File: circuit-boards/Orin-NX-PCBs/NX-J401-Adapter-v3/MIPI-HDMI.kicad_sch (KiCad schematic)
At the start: 2 parts, among them J10 MIPI, J11 HDMI

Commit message: Interim checkin of NX Adapter board
Signed-off-by: Scott Berman <scott.berman@bluerivertech.com>
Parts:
- J11: footprint NX-J401-Adapter:HDMI_A_Molex_208658-1001_Horizontal -> NX-J401-Adapter:SWITCHCRAFT_RAVHD19ETR; DIST P/N 900-2086581051CT-ND -> 137-RAVHD19ECT-ND; MFG Molex -> Switchcraft; MFG P/N 2086581051 -> RAVHD19ETR
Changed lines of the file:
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@@
 			)
 		)
-		(property "Footprint" "NX-J401-Adapter:HDMI_A_Molex_208658-1001_Horizontal"
+		(property "Footprint" "NX-J401-Adapter:SWITCHCRAFT_RAVHD19ETR"
 			(at 278.765 120.65 0)
 			(effects
@@
 			)
 		)
-		(property "Datasheet" "Components/Molex-HDMI-A-2086581051_sd.pdf"
+		(property "Datasheet" "Components/Switchcraft-RAVHD19ETR_CD.pdf"
 			(at 278.765 120.65 0)
 			(effects
@@
 			)
 		)
-		(property "Description" ""
+		(property "Description" "HDMI HDMI 2.0 Receptacle Connector 19 Position Through Hole, Right Angle"
 			(at 278.13 120.65 0)
 			(effects
@@
 			)
 		)
-		(property "MFG" "Molex"
+		(property "MFG" "Switchcraft"
 			(at 278.13 120.65 0)
 			(effects
@@
 			)
 		)
-		(property "MFG P/N" "2086581051"
+		(property "MFG P/N" "RAVHD19ETR"
 			(at 278.13 120.65 0)
 			(effects
@@
 			)
 		)
-		(property "DIST P/N" "900-2086581051CT-ND"
+		(property "DIST P/N" "137-RAVHD19ECT-ND"
 			(at 278.13 120.65 0)
 			(effects

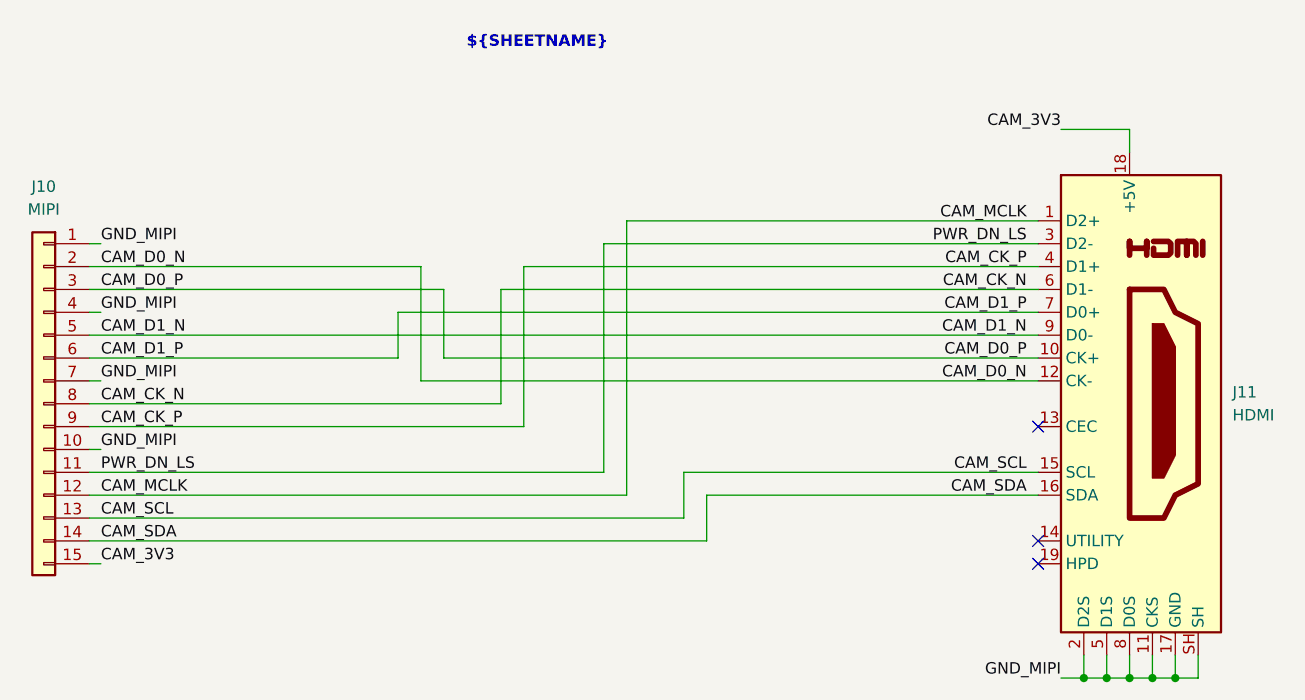
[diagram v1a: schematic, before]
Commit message: Check in of NX Adapter and Indicator boards.  Complete pending review
Signed-off-by: Scott <sgberman1@gmail.com>
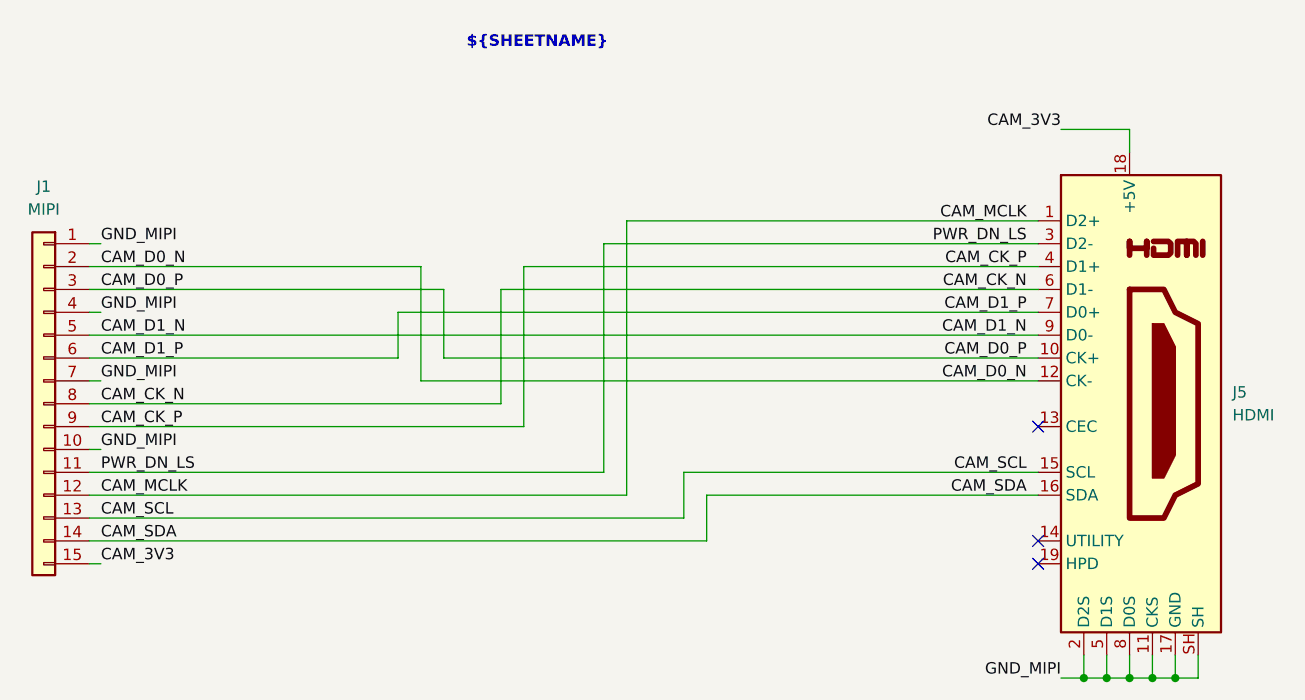
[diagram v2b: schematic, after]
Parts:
- renumbered J10 to J1, J11 to J5
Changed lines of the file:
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@@
 		(dnp no)
 		(fields_autoplaced yes)
-		(property "Reference" "J10"
+		(property "Reference" "J1"
 			(at 157.48 96.52 0)
 			(effects
@@
 			(project "NX-J401-Adapter"
 				(path "/cc31ce4b-09ab-4aea-a1d3-ed84696ba658/d1baeb55-0358-48eb-b719-8b69397a20ee"
-					(reference "J10")
+					(reference "J1")
 					(unit 1)
 				)
 				(path "/cc31ce4b-09ab-4aea-a1d3-ed84696ba658/ef5bdea0-feaa-4250-9b61-8c5edbd568c2"
-					(reference "J8")
+					(reference "J2")
 					(unit 1)
 				)
@@
 		(dnp no)
 		(fields_autoplaced yes)
-		(property "Reference" "J11"
+		(property "Reference" "J5"
 			(at 289.56 119.38 0)
 			(effects
@@
 			(project "NX-J401-Adapter"
 				(path "/cc31ce4b-09ab-4aea-a1d3-ed84696ba658/d1baeb55-0358-48eb-b719-8b69397a20ee"
-					(reference "J11")
+					(reference "J5")
 					(unit 1)
 				)
 				(path "/cc31ce4b-09ab-4aea-a1d3-ed84696ba658/ef5bdea0-feaa-4250-9b61-8c5edbd568c2"
-					(reference "J9")
-					(unit 1)
-				)
+					(reference "J3")
+					(unit 1)
+				)

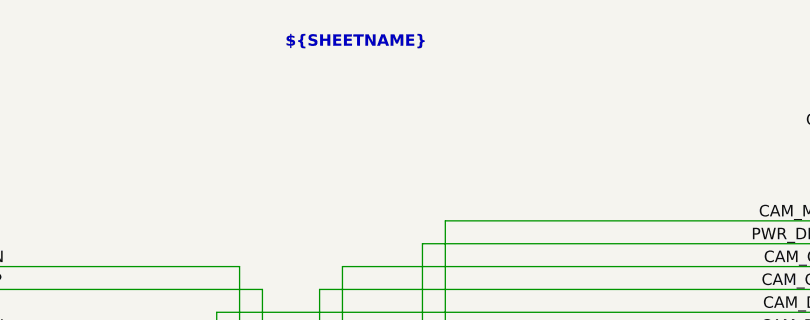
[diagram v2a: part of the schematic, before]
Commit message: Minor update to NX-J401-Adapter-v3
Signed-off-by: Scott Berman <scott.berman@bluerivertech.com>
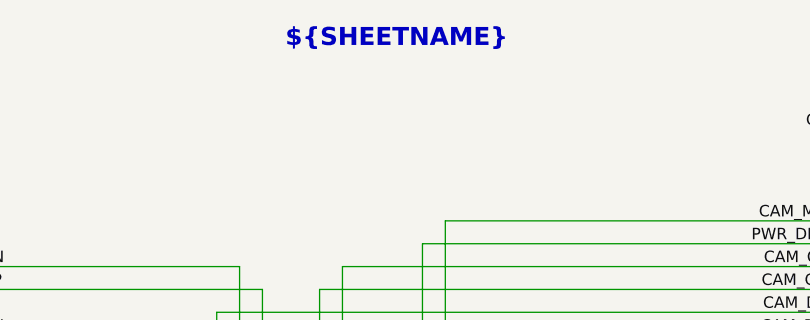
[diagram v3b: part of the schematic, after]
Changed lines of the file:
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@@
 	(title_block
 		(title "NX J401 Adapter")
-		(date "2023-06-04")
-		(rev "1")
+		(date "2024-08-05")
+		(rev "3")
 		(company "971 Spartan Robotics")
 	)
@@
 		(effects
 			(font
-				(size 1.27 1.27)
+				(size 2 2)
 				(bold yes)
 			)

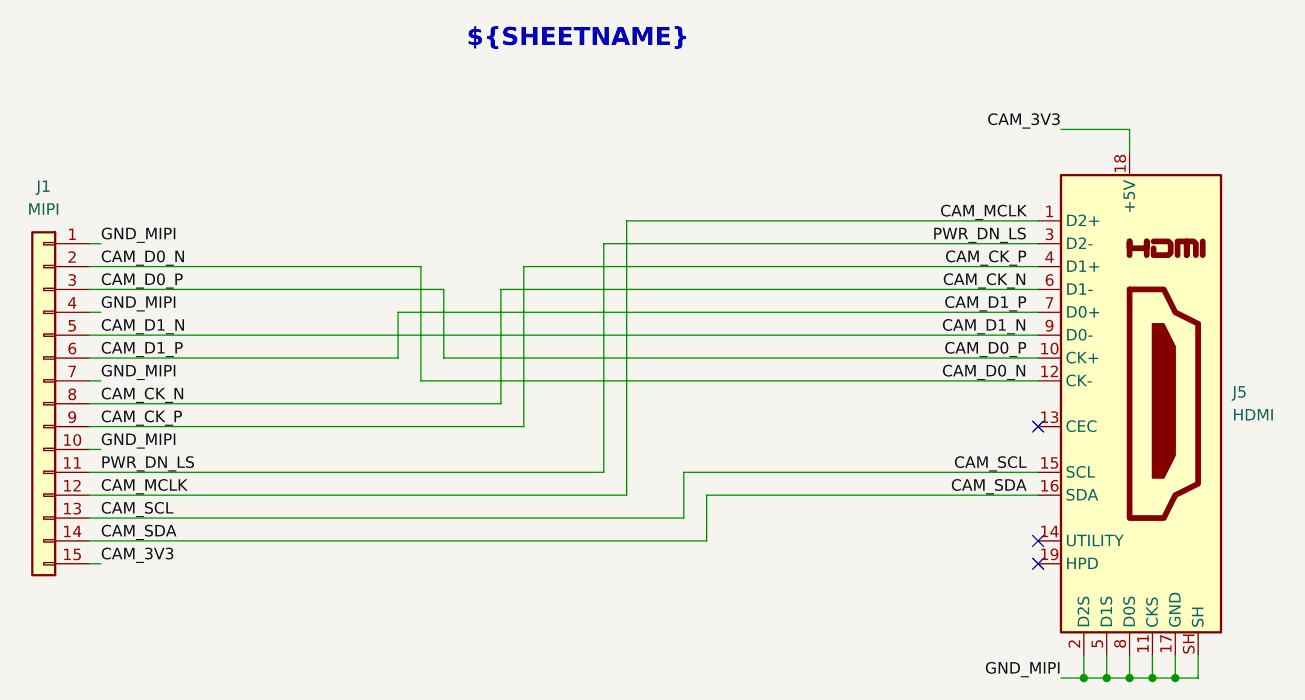
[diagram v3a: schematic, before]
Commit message: Updated diff pairs and power supply layout
Signed-off-by: Scott <sgberman1@gmail.com>
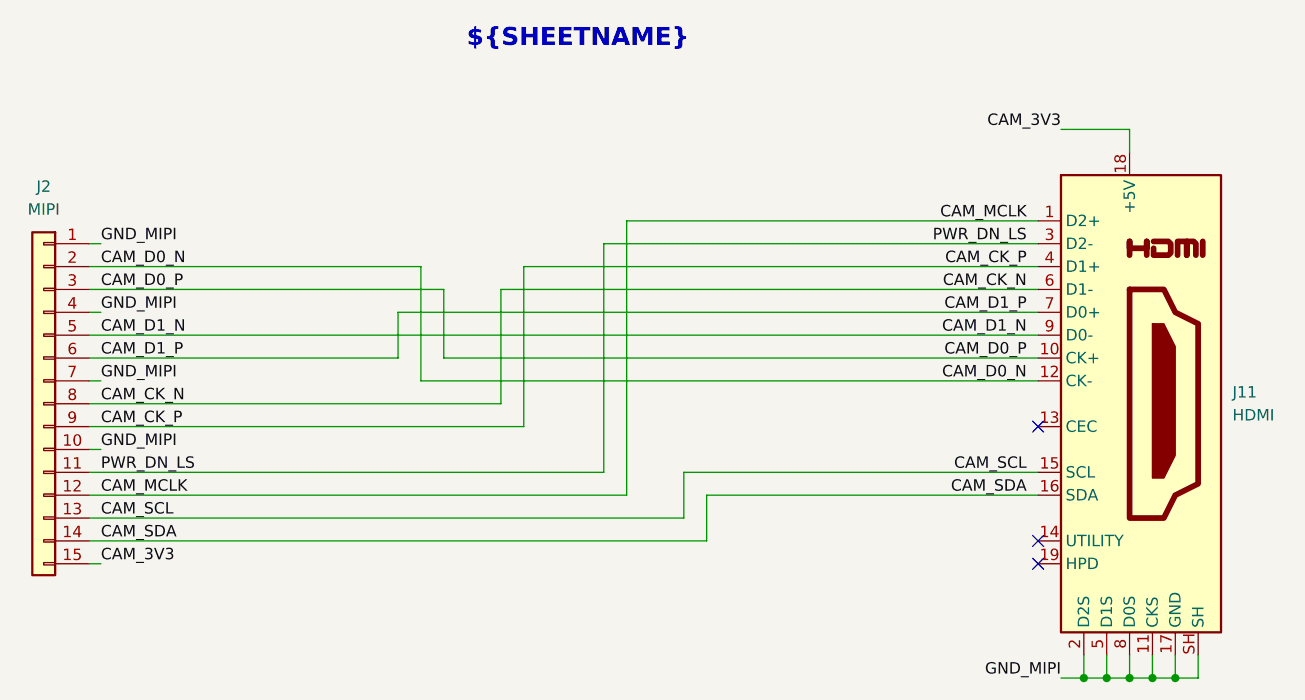
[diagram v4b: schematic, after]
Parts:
- renumbered J5 to J11, J1 to J2
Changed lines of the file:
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@@
 	(title_block
 		(title "NX J401 Adapter")
-		(date "2024-08-05")
+		(date "2024-08-10")
 		(rev "3")
 		(company "971 Spartan Robotics")
@@
 		(dnp no)
 		(fields_autoplaced yes)
-		(property "Reference" "J1"
+		(property "Reference" "J2"
 			(at 157.48 96.52 0)
 			(effects
@@
 			(project "NX-J401-Adapter"
 				(path "/cc31ce4b-09ab-4aea-a1d3-ed84696ba658/d1baeb55-0358-48eb-b719-8b69397a20ee"
-					(reference "J1")
+					(reference "J2")
 					(unit 1)
 				)
 				(path "/cc31ce4b-09ab-4aea-a1d3-ed84696ba658/ef5bdea0-feaa-4250-9b61-8c5edbd568c2"
-					(reference "J2")
+					(reference "J4")
 					(unit 1)
 				)
@@
 		(dnp no)
 		(fields_autoplaced yes)
-		(property "Reference" "J5"
+		(property "Reference" "J11"
 			(at 289.56 119.38 0)
 			(effects
@@
 			(project "NX-J401-Adapter"
 				(path "/cc31ce4b-09ab-4aea-a1d3-ed84696ba658/d1baeb55-0358-48eb-b719-8b69397a20ee"
-					(reference "J5")
+					(reference "J11")
 					(unit 1)
 				)
 				(path "/cc31ce4b-09ab-4aea-a1d3-ed84696ba658/ef5bdea0-feaa-4250-9b61-8c5edbd568c2"
-					(reference "J3")
+					(reference "J10")
 					(unit 1)
 				)
